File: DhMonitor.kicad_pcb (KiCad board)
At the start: 2 copper layers, 8 parts, among them J1 ProMiniDTRSide, J2 A4A5, J3 PowerRaw, J4 ProMiniRawSide, J5 RTC, J6 sdCardReader

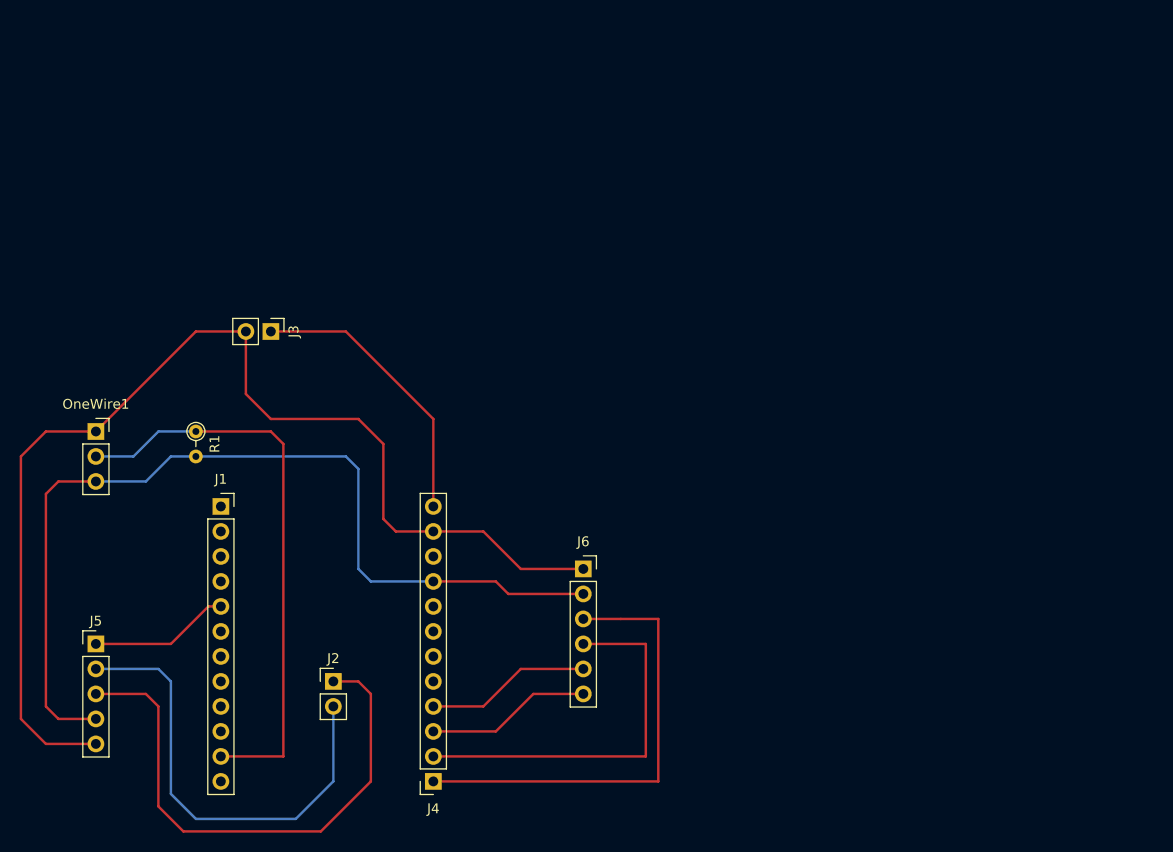
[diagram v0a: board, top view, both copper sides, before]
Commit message: solves wrong files :o
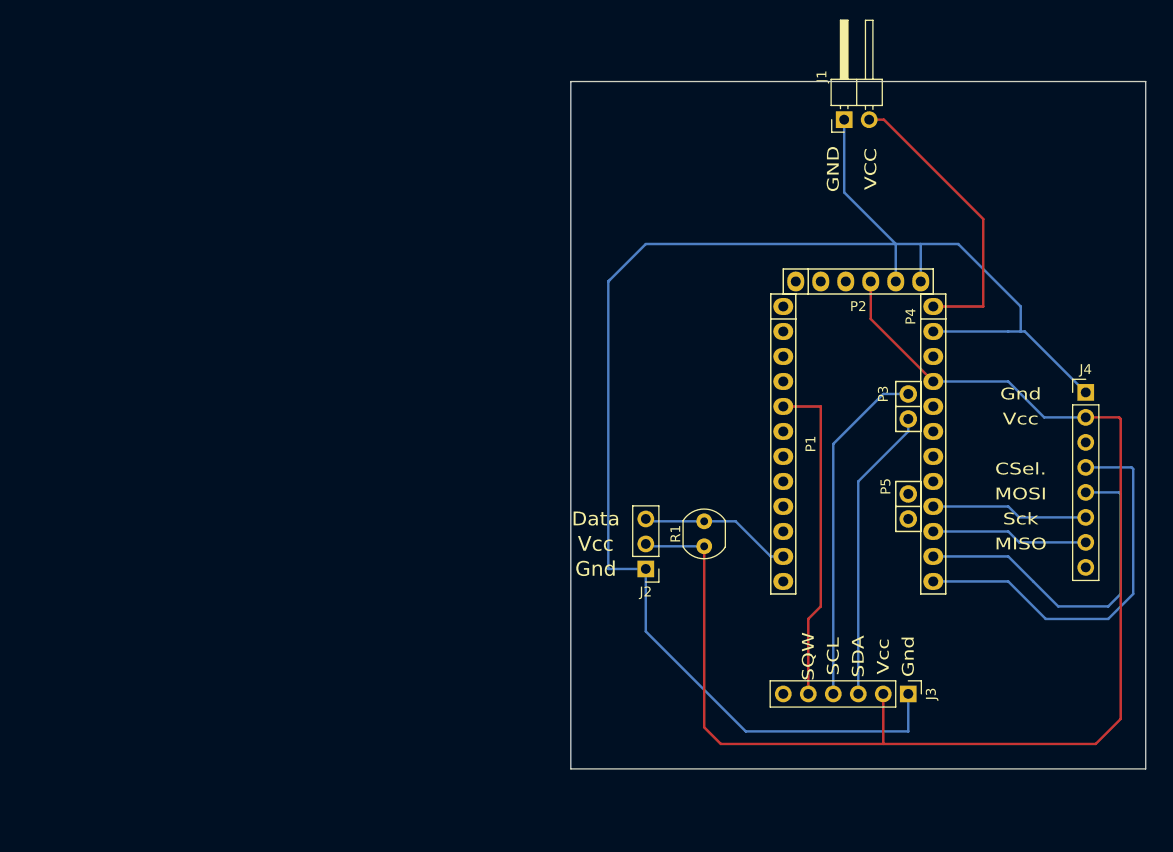
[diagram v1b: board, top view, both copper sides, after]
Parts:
- removed J5: RTC, Connector_PinHeader_2.54mm:PinHeader_1x05_P2.54mm_Vertical
- removed J6: sdCardReader, Connector_PinSocket_2.54mm:PinSocket_1x06_P2.54mm_Vertical
- removed OneWire1: Conn_01x03, Connector_PinSocket_2.54mm:PinSocket_1x03_P2.54mm_Vertical
- added P1: Digital, Socket_Arduino_Pro_Mini:Socket_Strip_Arduino_1x12, F.Cu at (138.4, 85.1)
- added P2: COM, Socket_Arduino_Pro_Mini:Socket_Strip_Arduino_1x06, F.Cu at (139.7, 82.5)
- added P3: ADC, Socket_Arduino_Pro_Mini:Socket_Strip_Arduino_1x02, F.Cu at (151.1, 94.0)
- added P4: Analog, Socket_Arduino_Pro_Mini:Socket_Strip_Arduino_1x12, F.Cu at (153.7, 85.1)
- added P5: ADC, Socket_Arduino_Pro_Mini:Socket_Strip_Arduino_1x02, F.Cu at (151.1, 104.1)
- J1: value ProMiniDTRSide -> Power; footprint Connector_PinSocket_2.54mm:PinSocket_1x12_P2.54mm_Vertical -> Connector_PinHeader_2.54mm:PinHeader_1x02_P2.54mm_Horizontal
- J2: value A4A5 -> DS18B20; footprint Connector_PinHeader_2.54mm:PinHeader_1x02_P2.54mm_Vertical -> Connector_PinHeader_2.54mm:PinHeader_1x03_P2.54mm_Vertical
- J3: value PowerRaw -> RTC; footprint Connector_PinHeader_2.54mm:PinHeader_1x02_P2.54mm_Vertical -> Connector_PinHeader_2.54mm:PinHeader_1x06_P2.54mm_Vertical
- J4: value ProMiniRawSide -> SD Card Module; footprint Connector_PinSocket_2.54mm:PinSocket_1x12_P2.54mm_Vertical -> Connector_PinHeader_2.54mm:PinHeader_1x08_P2.54mm_Vertical
- R1: footprint Resistor_THT:R_Axial_DIN0204_L3.6mm_D1.6mm_P2.54mm_Vertical -> OptoDevice:R_LDR_4.9x4.2mm_P2.54mm_Vertical
- moved J4 77.2 mm to (169.2, 93.8), turned to 0 degrees
- moved J1 74.5 mm to (144.6, 66.1), turned to 90 degrees
- moved J3 74.5 mm to (151.1, 124.5)
- moved R1 53.0 mm to (130.4, 109.5), turned to 90 degrees
- moved J2 33.7 mm to (124.5, 111.8), turned to 180 degrees
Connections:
- J1 pad 2: Net-(J1-Pad2) -> /RAW
- J2 pad 1: Net-(J2-Pad1) -> Net-(J1-Pad1)
- J3 pad 1: /+ -> Net-(J1-Pad1)
- J3 pad 2: /GND -> Net-(J2-Pad2)
- J4 pad 1: Net-(J4-Pad1) -> Net-(J1-Pad1)
- J4 pad 2: Net-(J4-Pad2) -> Net-(J2-Pad2)
- J4 pad 5: Net-(J4-Pad5) -> /10(**/SS)
- J4 pad 6: Net-(J4-Pad6) -> /13(SCK)
- J4 pad 7: Net-(J4-Pad7) -> /12(MISO)
- R1 pad 1: Net-(J1-Pad11) -> Net-(J2-Pad2)
- R1 pad 2: Net-(J4-Pad9) -> /8
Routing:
- net Net-(J1-Pad1): track 0.00 -> 163.4 mm
- net /GND: track 115.9 -> 0.00 mm
- net Net-(J4-Pad9): track 95.1 -> 0.00 mm
- net Net-(J2-Pad2): track 46.3 -> 137.5 mm
- net Net-(J1-Pad11): track 58.7 -> 0.00 mm
- net Net-(J2-Pad1): track 55.0 -> 0.00 mm
- net Net-(J4-Pad1): track 47.0 -> 0.00 mm
- net Net-(J4-Pad2): track 39.4 -> 0.00 mm
- net /10(**/SS): track 0.00 -> 35.5 mm
- net /A5: track 0.00 -> 35.1 mm
- net /2: track 0.00 -> 33.5 mm
- net /A4: track 0.00 -> 30.0 mm
- net /RAW: track 0.00 -> 29.7 mm
- net /+: track 29.1 -> 0.00 mm
- net Net-(J4-Pad4): track 16.8 -> 40.5 mm
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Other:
- board outline added: 58.4 x 69.9 mm
- net class Default: via_dia 0.8 -> 0.6
- rule pad_to_mask_clearance: 0.051 -> 0
- board text added: "1"
- board text added: "CSel."
- board text added: "Data"
- board text added: "GND"
- board text added: "Gnd"
- board text added: "MISO"
- board text added: "MOSI"
- board text added: "SCL"
- board text added: "SDA"
- board text added: "SQW"
- board text added: "Sck"
- board text added: "VCC"
- board text added: "Vcc"

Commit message: v0.2: add labels + mounting holes + hx711 pinouts
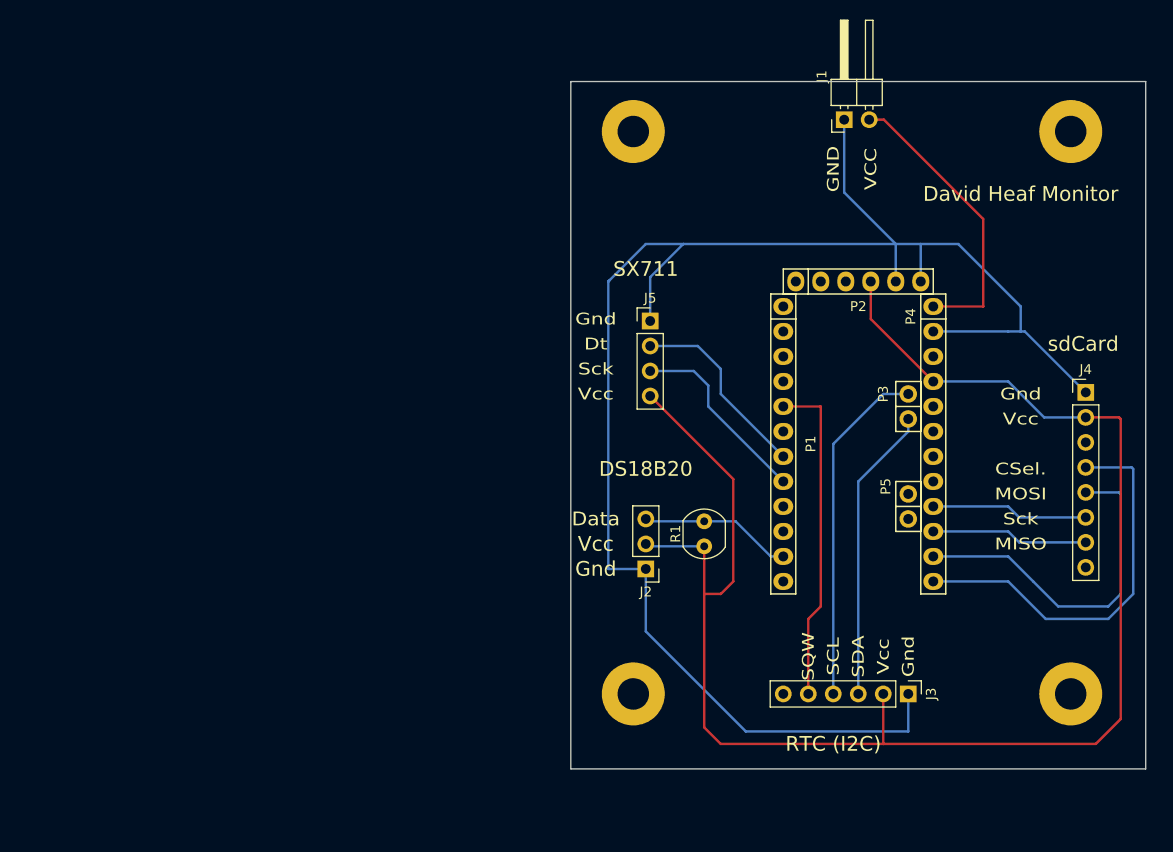
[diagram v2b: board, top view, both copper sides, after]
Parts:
- added J5: HX711, Connector_PinHeader_2.54mm:PinHeader_1x04_P2.54mm_Vertical, F.Cu at (124.9, 86.6)
- added REF**: MountingHole_3.2mm_M3_Pad, MountingHole:MountingHole_3.2mm_M3_Pad, F.Cu at (123.2, 67.3)
- added REF**: MountingHole_3.2mm_M3_Pad, MountingHole:MountingHole_3.2mm_M3_Pad, F.Cu at (167.6, 67.3)
- added REF**: MountingHole_3.2mm_M3_Pad, MountingHole:MountingHole_3.2mm_M3_Pad, F.Cu at (123.2, 124.5)
- added REF**: MountingHole_3.2mm_M3_Pad, MountingHole:MountingHole_3.2mm_M3_Pad, F.Cu at (167.6, 124.5)
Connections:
- net Net-(J1-Pad1) renamed /Gnd
- net Net-(J2-Pad2) renamed /Vcc
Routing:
- net /Vcc: track 137.5 -> 163.3 mm
- net /4: track 0.00 -> 19.7 mm
- net /5(**): track 0.00 -> 19.4 mm
- net /Gnd: track 163.4 -> 172.6 mm
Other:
- board text added: "DS18B20"
- board text added: "David Heaf Monitor"
- board text added: "Dt"
- board text added: "RTC (I2C)"
- board text added: "SX711"
- board text added: "sdCard"
